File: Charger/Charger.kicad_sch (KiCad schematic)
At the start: 27 parts, among them J1 PL00X-301-10M8, J2 PL00Y-301-10M8, K1 Gigavc PNC11BDA, K2 EV200 HAANA, SW1 Emergency Button, SW2 SW_Push, SW3 SW_Push, U1 ATmega328-A, Y1 20MHz

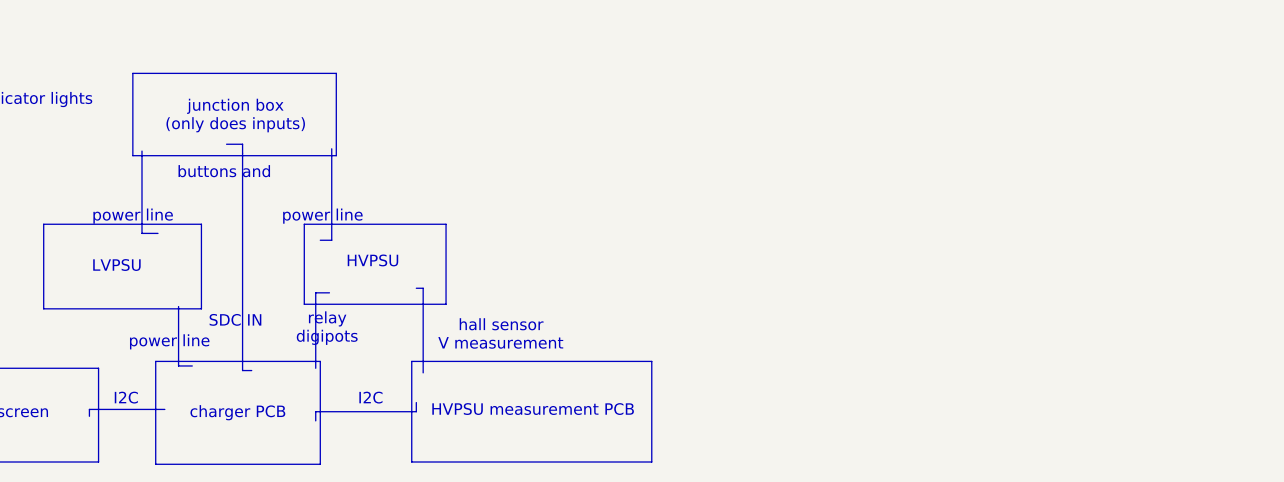
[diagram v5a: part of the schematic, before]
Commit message: charger moved to 10.0, a few notes added
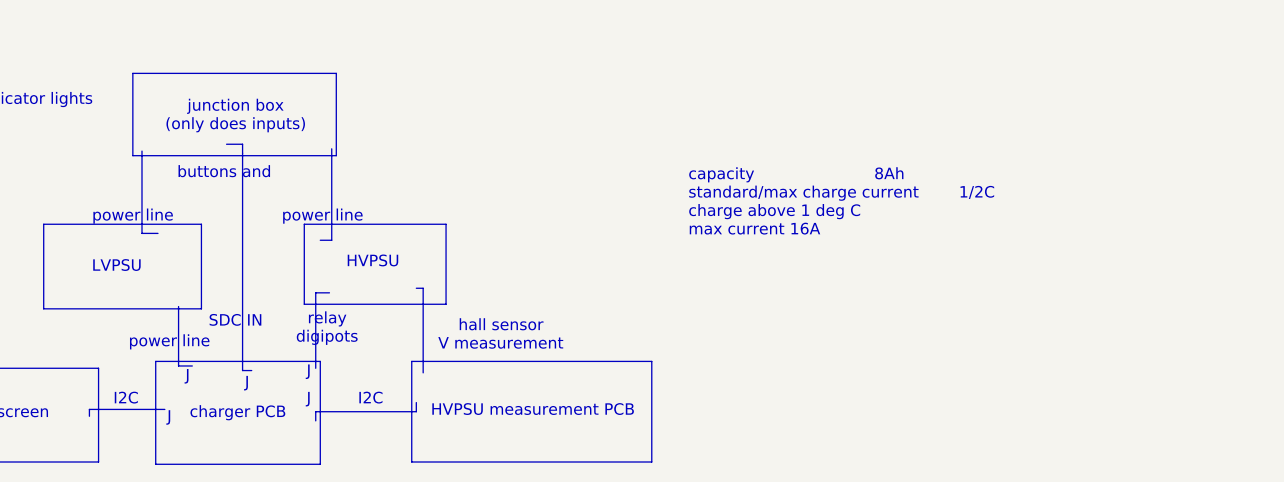
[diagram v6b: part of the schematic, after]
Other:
- note added: "capacity 8Ah standard/max charge current 1/2C charge above 1 deg C max current 16A"
